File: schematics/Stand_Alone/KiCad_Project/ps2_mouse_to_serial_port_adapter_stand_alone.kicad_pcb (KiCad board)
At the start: 2 copper layers, 91.4 x 71.1 mm, 28 parts, among them J1 Barrel Jack 2.1 mm, J2 DB9 Female, J3 Mini-DIN-6, Q1 BC547, SW1 1C2P, U1 74LS00, U2 L78L05, U3 L7805

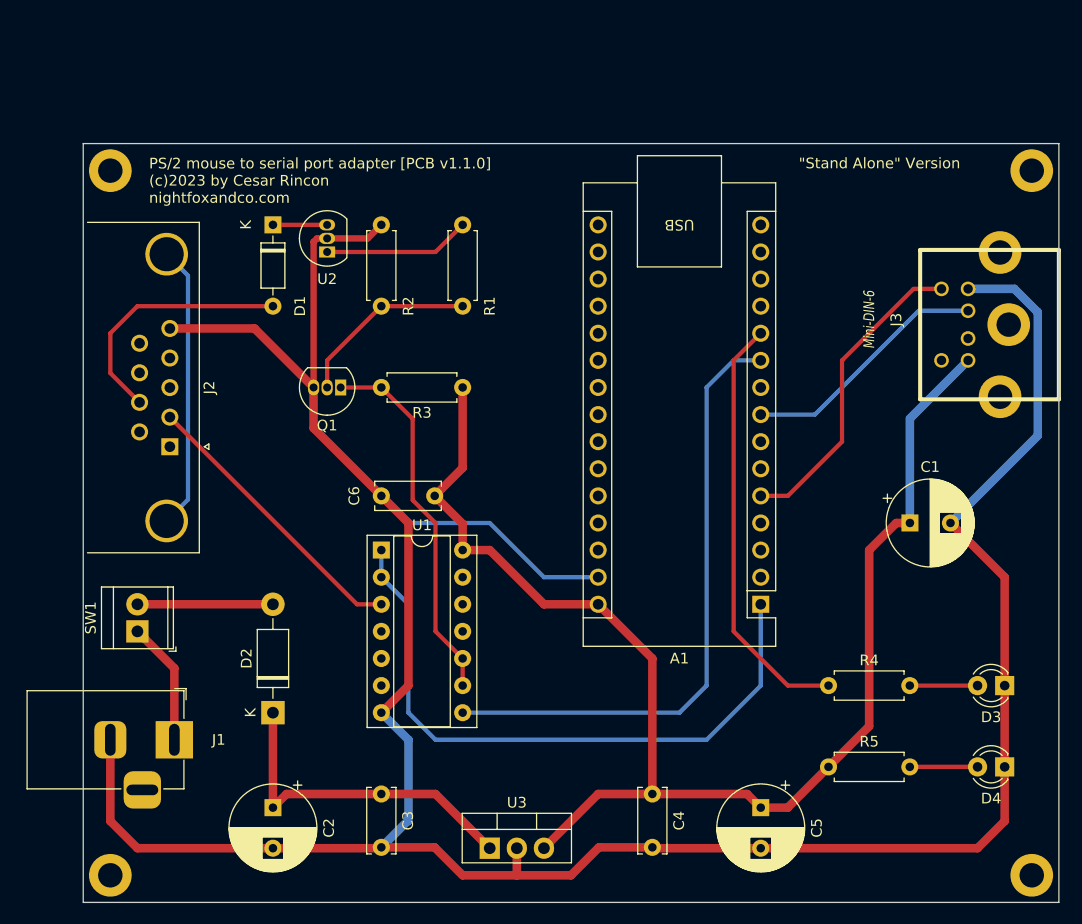
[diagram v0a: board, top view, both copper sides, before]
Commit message: v1.5.0
- Ajustadas las placas "Stand alone" y "In-a-box" al tamaño standard de
  90x70 mm.
- Añadidas a estas placas las zonas de relleno a masa (GND).
- Añadidas las serigrafias con los valores de todos los componentes en todas
  las versiones de las placas.
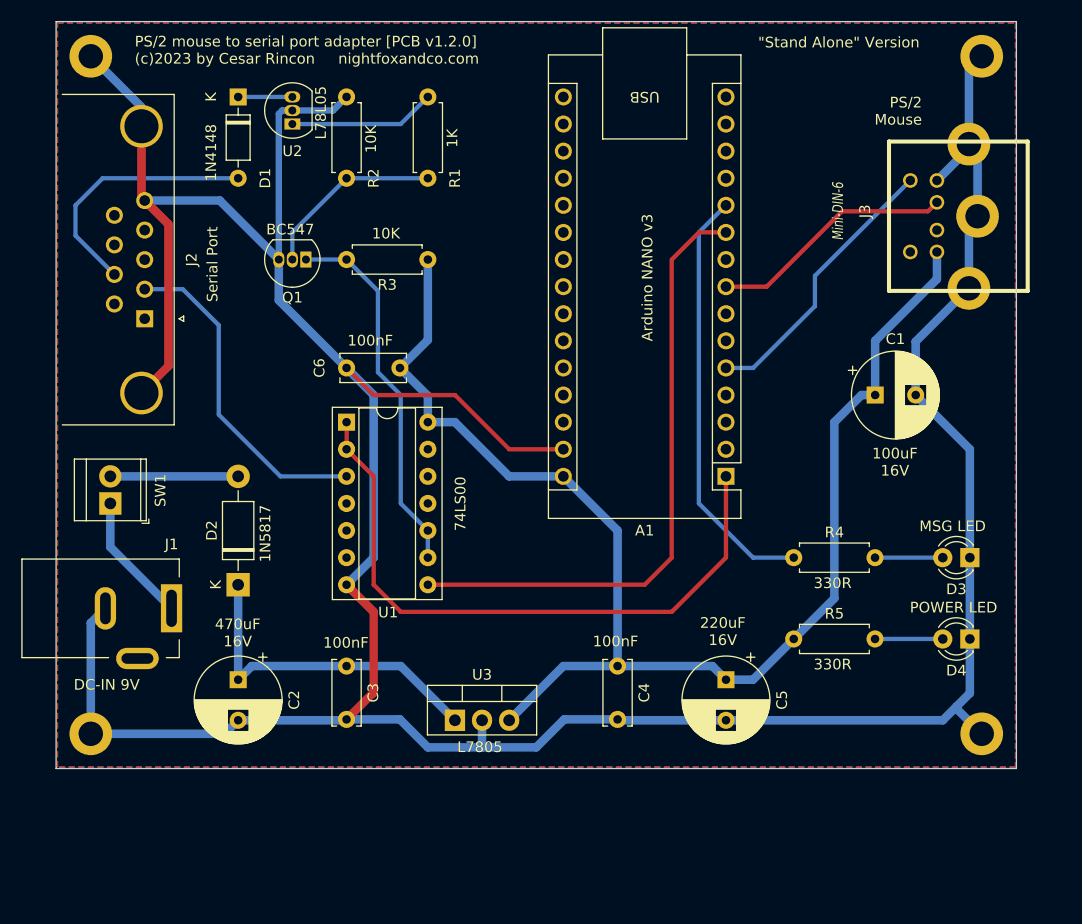
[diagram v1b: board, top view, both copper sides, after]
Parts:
- J1: value Barrel Jack 2.1 mm -> 2.1 Barrel Jack; footprint Connector_BarrelJack:BarrelJack_Horizontal -> Connector_BarrelJack:BarrelJack_Kycon_KLDX-0202-xC_Horizontal
- moved ? 12.4 mm to (24.7, 82.0)
- moved D3 12.4 mm to (108.5, 64.2)
- moved R4 12.4 mm to (92.0, 64.2)
- moved ? 12.4 mm to (111.0, 82.0)
- moved C6 12.4 mm to (55.1, 46.4)
- moved R2 12.4 mm to (50.1, 28.6)
- moved U1 12.4 mm to (50.1, 51.5)
- moved ? 12.4 mm to (24.7, 15.9)
- moved ? 12.4 mm to (111.0, 15.9)
- moved C1 12.4 mm to (99.6, 49.0)
- moved D1 12.4 mm to (39.9, 21.0)
- moved R1 12.4 mm to (57.7, 28.6)
- moved U2 12.4 mm to (45.0, 23.6)
- moved A1 12.4 mm to (85.6, 56.6)
- moved C3 12.4 mm to (50.1, 74.4)
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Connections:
- net Net-(A1-VIN) renamed /+5V
- ? pad GND: (no net) -> /GND (x4)
- A1 pad 29: Net-(D3-K) -> /GND
- C1 pad 2: Net-(D3-K) -> /GND
- C2 pad 2: Net-(D3-K) -> /GND
- C3 pad 2: Net-(D3-K) -> /GND
- C4 pad 2: Net-(D3-K) -> /GND
- C5 pad 2: Net-(D3-K) -> /GND
- C6 pad 2: Net-(D3-K) -> /GND
- D3 pad 1: Net-(D3-K) -> /GND
- D4 pad 1: Net-(D3-K) -> /GND
- J1 pad 2: Net-(D3-K) -> /GND
- J1 pad 3: (no net) -> unconnected-(J1-MountPin-Pad3)
- J2 pad 0: unconnected-(J2-PAD-Pad0) -> /GND
- J2 pad 5: Net-(D3-K) -> /GND
- J3 pad 3: Net-(D3-K) -> /GND
- J3 pad GND: (no net) -> /GND
- Q1 pad 3: Net-(D3-K) -> /GND
- R2 pad 2: Net-(D3-K) -> /GND
- U1 pad 7: Net-(D3-K) -> /GND
- U2 pad 2: Net-(D3-K) -> /GND
- U3 pad 2: Net-(D3-K) -> /GND
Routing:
- net /GND: track 0.00 -> 313.7 mm
- net Net-(D3-K): track 268.8 -> 0.00 mm
- net unconnected-(J2-PAD-Pad0): track 26.7 -> 0.00 mm
- net Net-(J2-Pad2): track 27.1 -> 31.1 mm
- net Net-(A1-D2): track 29.4 -> 26.2 mm
- net /+5V: track 127.3 -> 125.6 mm
- net Net-(D2-A): track 12.7 -> 12.0 mm
- net Net-(SW1-A): track 11.6 -> 12.2 mm
- added copper zone on B.Cu, net /GND
- added copper zone on F.Cu, net /GND
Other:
- board size 91.4 x 71.1 mm -> 90 x 70 mm
- board text added: "100nF"
- board text added: "100uF 16V"
- board text added: "10K"
- board text added: "1K"
- board text added: "1N4148"
- board text added: "1N5817"
- board text added: "220uF 16V"
- board text added: "330R"
- board text added: "470uF 16V"
- board text added: "74LS00"
- board text added: "Arduino NANO v3"
- board text added: "BC547"
- board text added: "DC-IN 9V"
- board text added: "L7805"
- board text added: "L78L05"
- board text added: "MSG LED"
- board text added: "POWER LED"
- board text added: "PS/2 Mouse"
- board text added: "PS/2 mouse to serial port adapter [PCB v1.2.0] (c)2023 by Cesar Rincon nightfoxandco.com"
- board text added: "Serial Port"
- board text removed: "PS/2 mouse to serial port adapter [PCB v1.1.0] (c)2023 by Cesar Rincon nightfoxandco.com"

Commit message: v1.5.1
- Arreglada la serigrafía del conector MINI-DIN-6 (PS/2), la cual se superponía en algunas zonas de soldado.
- En todas las placas se añade el símbolo de los agujeros de montaje con el tamaño estándar M3.
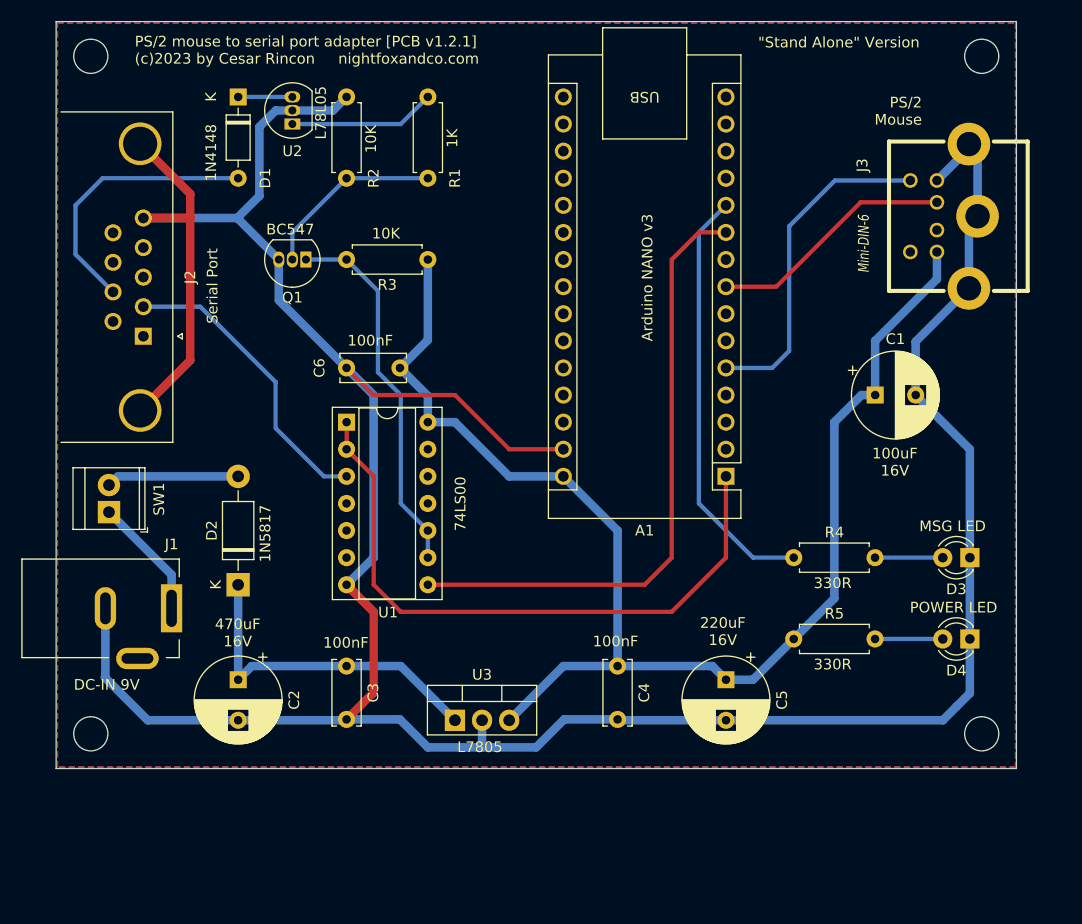
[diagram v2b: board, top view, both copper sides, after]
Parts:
- removed ? (x4): , 
- added H1: MountingHole, MountingHole:MountingHole_3.2mm_M3, F.Cu at (26.1, 17.2)
- added H2: MountingHole, MountingHole:MountingHole_3.2mm_M3, F.Cu at (109.6, 17.2)
- added H3: MountingHole, MountingHole:MountingHole_3.2mm_M3, F.Cu at (26.1, 80.7)
- added H4: MountingHole, MountingHole:MountingHole_3.2mm_M3, F.Cu at (109.6, 80.7)
- J3: footprint CustomFootPrints:Conn_Mini_DIN_6pin -> ProjectLibrary:Connector_Mini_DIN_6pin
- moved J2 1.64 mm to (31.0, 43.5)
- moved SW1 0.82 mm to (27.8, 59.9)
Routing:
- net /GND: track 313.7 -> 293.1 mm
- net Net-(A1-D2): track 26.2 -> 31.4 mm
- net Net-(J2-Pad2): track 31.1 -> 28.2 mm
- net Net-(D1-A): track 24.3 -> 25.9 mm
- net Net-(SW1-A): track 12.2 -> 11.4 mm
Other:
- board text added: "PS/2 mouse to serial port adapter [PCB v1.2.1] (c)2023 by Cesar Rincon nightfoxandco.com"
- board text removed: "PS/2 mouse to serial port adapter [PCB v1.2.0] (c)2023 by Cesar Rincon nightfoxandco.com"

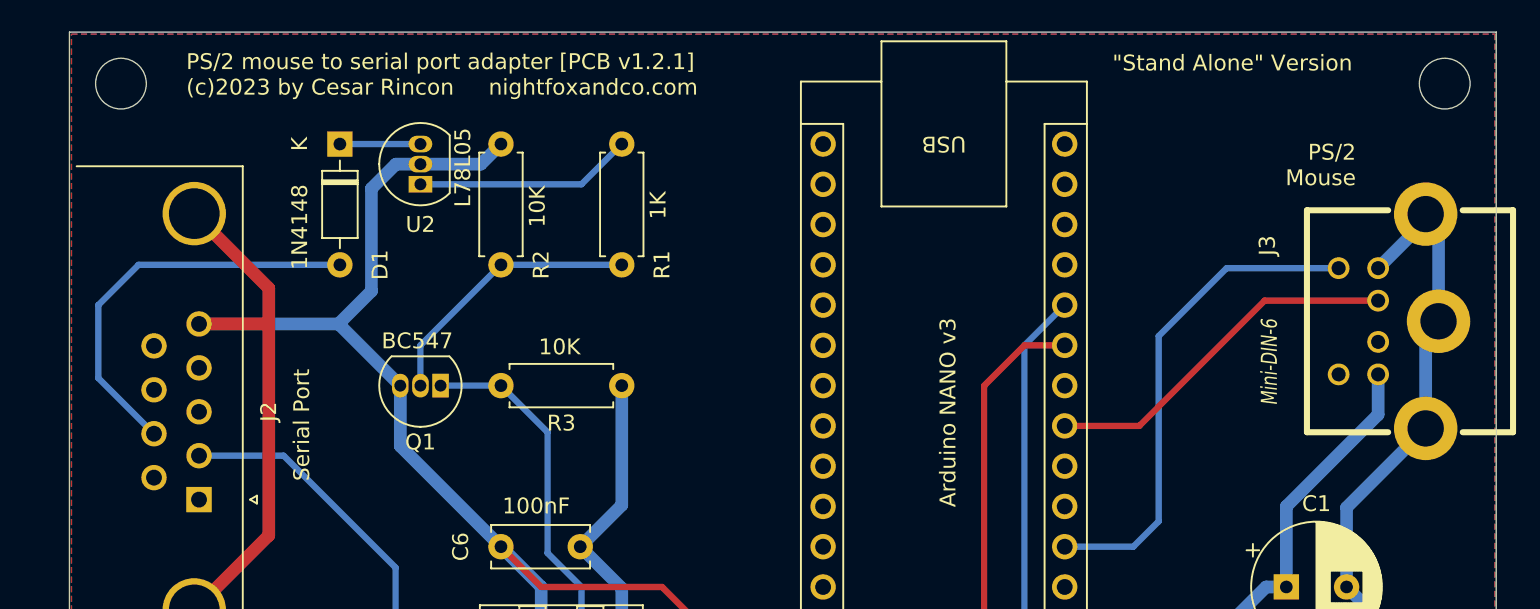
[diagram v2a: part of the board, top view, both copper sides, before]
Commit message: v1.7.0
- Modificadas las huellas de todas las placas para que los componentes TO92 resulten más fáciles de soldar a mano.
- Modificadas las conexiones del conector IDC en la placa ISA para poder usar un cable IDC a DB9 comercial, sin necesidad de realizarle modificaciones.
- Añadido el modelo en formato FreeCad y el archivo STL del soporte para la placa ISA. Estos archivos estan preparados para poder realizar la impresión en 3D del soporte. Se recomienda un in-fill del 100%.
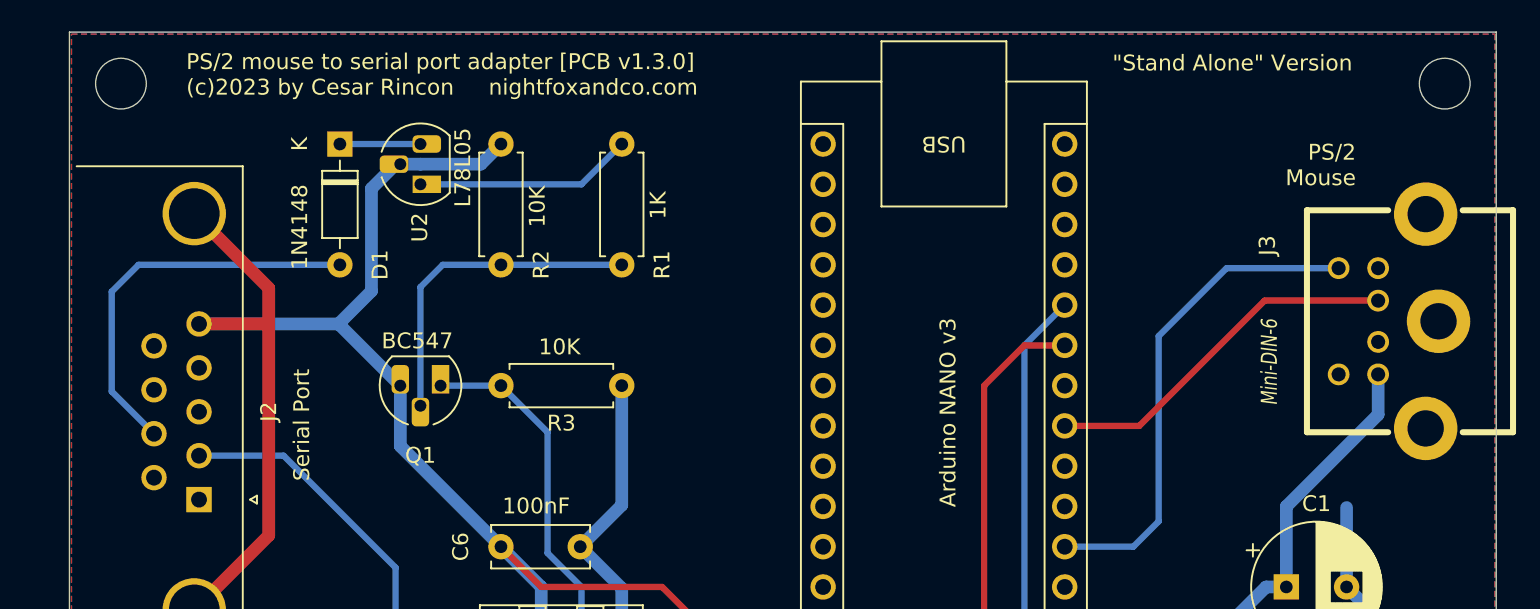
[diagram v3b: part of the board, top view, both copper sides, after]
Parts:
- Q1, U2: footprint Package_TO_SOT_THT:TO-92_Inline -> Package_TO_SOT_THT:TO-92_HandSolder
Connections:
- J3 pad GND: /GND -> (no net)
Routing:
- net /GND: track 293.1 -> 269.9 mm
- net Net-(Q1-B): track 17.3 -> 20.8 mm
- net Net-(D1-A): track 25.9 -> 25.2 mm
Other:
- board text added: "PS/2 mouse to serial port adapter [PCB v1.3.0] (c)2023 by Cesar Rincon nightfoxandco.com"
- board text removed: "PS/2 mouse to serial port adapter [PCB v1.2.1] (c)2023 by Cesar Rincon nightfoxandco.com"
